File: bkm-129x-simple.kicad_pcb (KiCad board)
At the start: 2 copper layers, 105 x 160 mm, 55 parts, among them J1 YG_IN, J11 YG_OUT, J2 PBB_IN, J21 PBB_OUT, J3 PRR_IN, J31 PRR_OUT, J4 SYNC_IN, J41 SYNC_OUT, J5 Conn_02x32_Row_Letter_Last, Q1 DTC144EKA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

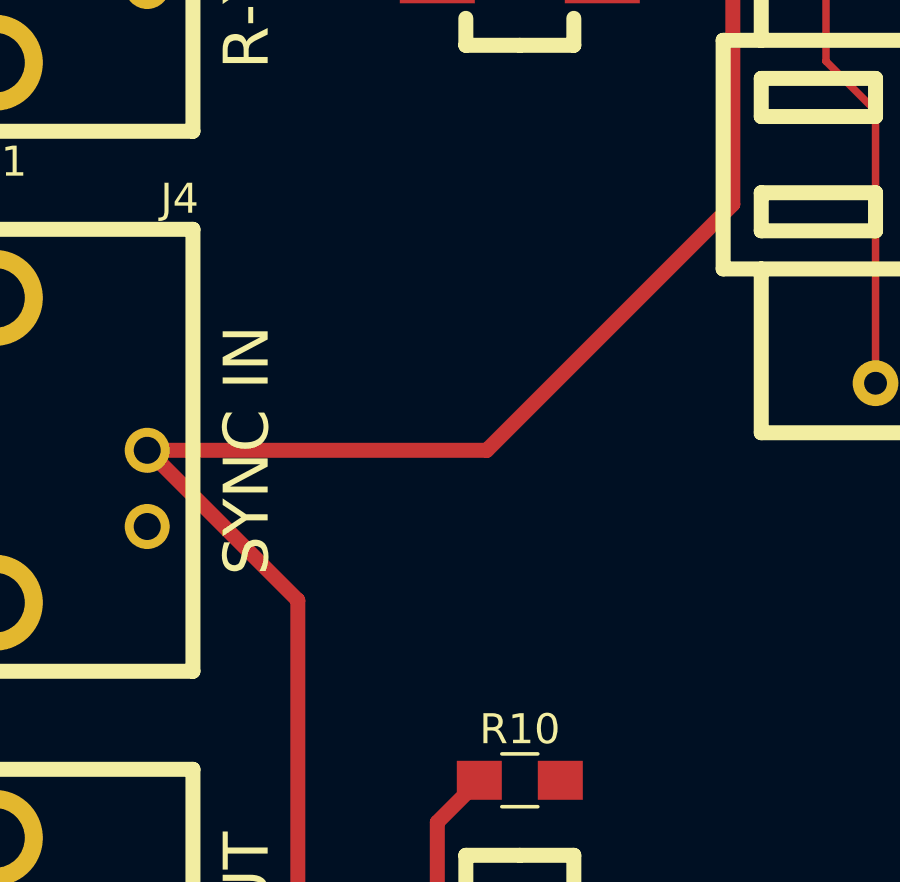
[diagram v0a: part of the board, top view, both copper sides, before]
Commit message: Add sync level info
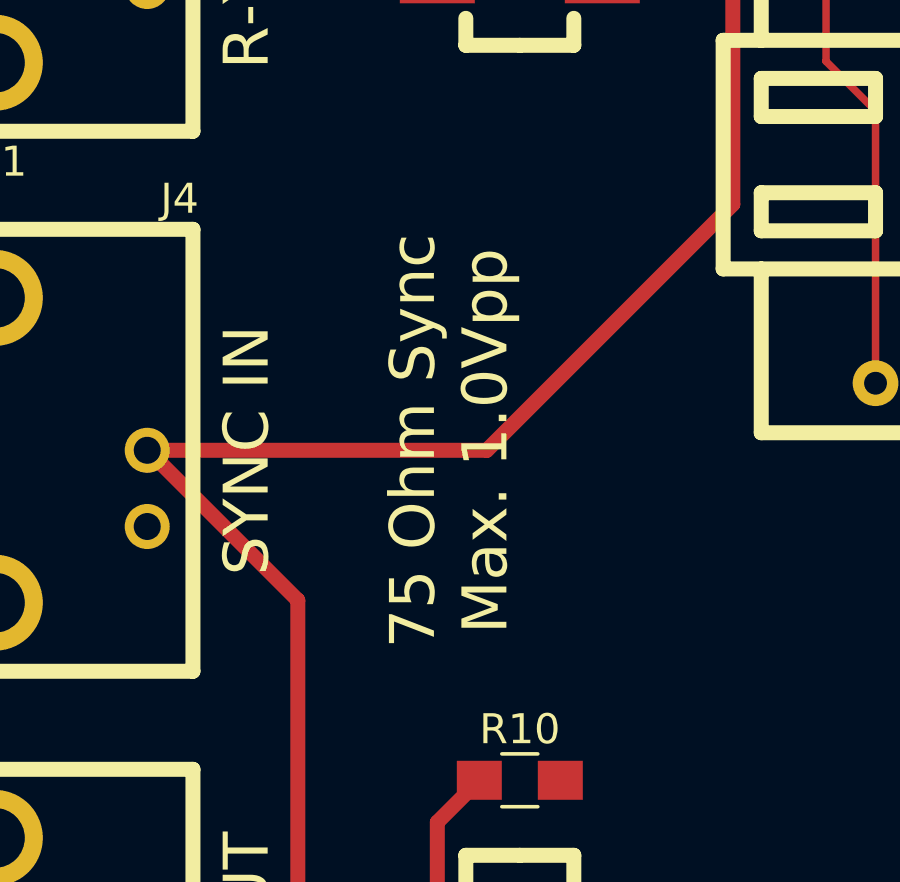
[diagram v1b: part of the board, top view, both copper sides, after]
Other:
- board text added: "75 Ohm Sync Max. 1.0Vpp"
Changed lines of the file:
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@@
     (area 73.555999 43.324999 201.918 203.475001)
     (thickness 1.6)
-    (drawings 25)
+    (drawings 26)
     (tracks 432)
     (zones 0)
@@
     (pad 4 smd rect (at -2.5 -2.75 270) (size 1.2 2.5) (layers F.Cu F.Paste F.Mask))
   )
+  (gr_text "75 Ohm Sync\nMax. 1.0Vpp" (at 117.35 168.09 90) (layer F.SilkS)
+    (effects (font (size 1.5 1.5) (thickness 0.3)))
+  )
   (gr_text "ON (75R TERM)\n\nOFF (PASSTHROUGH)" (at 126.2 78.4) (layer F.SilkS)

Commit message: Rev B: Added onboard MCU
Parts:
- added C15: 1uF, Capacitors_SMD:C_0805_HandSoldering, F.Cu at (140.8, 161.5)
- added C16: 4.7uF, Capacitors_SMD:C_0805_HandSoldering, F.Cu at (157.6, 155.4)
- added C17: 100nF, Capacitors_SMD:C_0805_HandSoldering, F.Cu at (142.0, 163.7)
- added J6: ICSP, Pin_Headers:Pin_Header_Straight_2x03_Pitch2.54mm, F.Cu at (168.9, 161.1)
- added U6: ATMEGA328PB-AU, Housings_QFP:TQFP-32_7x7mm_Pitch0.8mm, F.Cu at (149.3, 158.5)
- added Y1: CSTNE16M0VH3L000R0, muRata-CSTNEx:CSTNEx, F.Cu at (153.6, 153.2)
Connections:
- net /MCU_SCK renamed MCU_SCK
- net /MCU_SLOT_ID renamed MCU_SLOT_ID
- net /~MCU_RESET renamed ~MCU_RESET
- net Net-(R23-Pad1) renamed MCU_MISO
- net Net-(U3-Pad13) renamed ~MCU_SS
- net Net-(U3-Pad14) renamed MCU_MOSI
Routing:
- net MCU_SCK: track 42.1 -> 110.1 mm
- net MCU_MISO: track 30.6 -> 73.1 mm, vias 1 -> 2
- net MCU_MOSI: track 16.0 -> 53.3 mm, vias 0 -> 1
- net +5VD: track 102.4 -> 136.2 mm
- net ~MCU_RESET: track 17.8 -> 39.4 mm
- net ~MCU_SS: track 25.3 -> 36.5 mm
- net MCU_SLOT_ID: track 21.3 -> 31.0 mm, vias 1 -> 2
- net Net-(U6-Pad7): track 0.00 -> 5.31 mm
- net ~EXT_SYNC_OE: track 35.5 -> 40.4 mm
- net Net-(C17-Pad2): track 0.00 -> 4.14 mm
- net ~BX_OE: track 46.4 -> 49.9 mm
- net Net-(U6-Pad8): track 0.00 -> 3.21 mm
- net GND: track 10.6 -> 11.9 mm, vias 8 -> 9
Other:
- board text added: "ICSP"
- board text added: "Only mount inside this area, if NOT using a premade Arduino Nano board! U6 - ATMEGA328PB-AU Y1 - CSTNE16M0VH3L000R0 (16MHz resonator, GND in middle) C15 - 1 uF C16 - 4.7 uF C17 - 0.1 uF"
- board text added: "Rev. B"
- board text removed: "Rev. A"

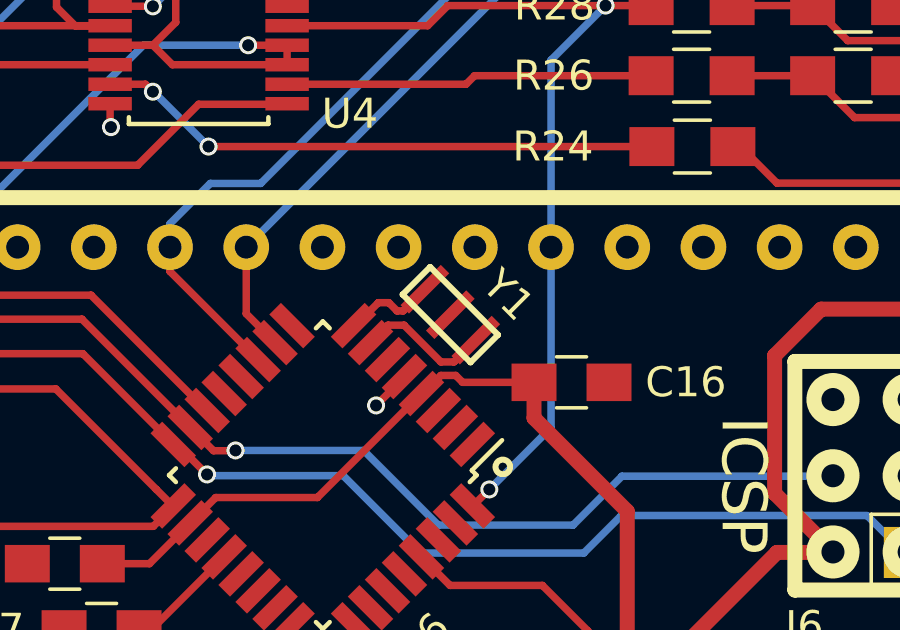
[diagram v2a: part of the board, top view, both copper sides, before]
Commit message: Add onboard ATMEGA328PB
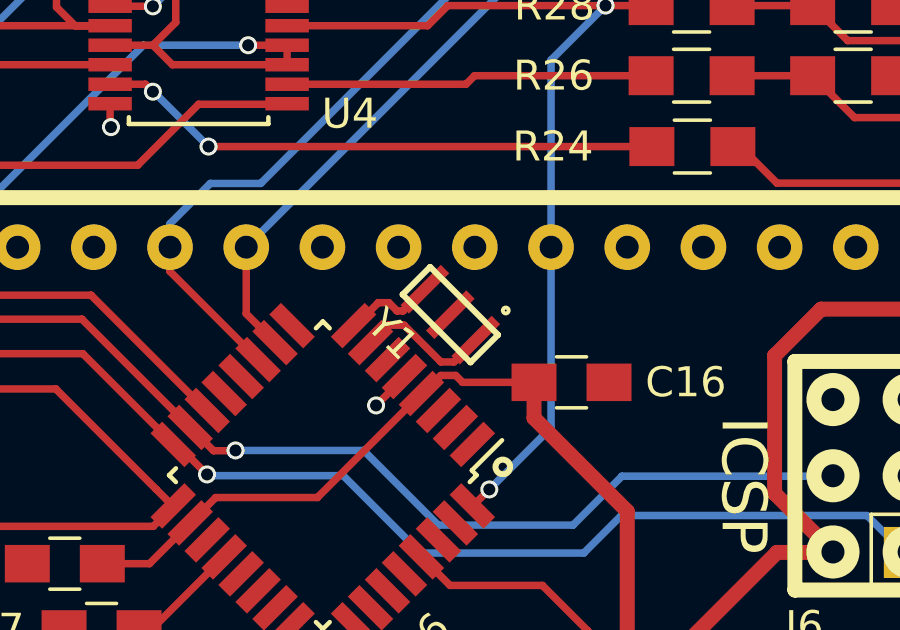
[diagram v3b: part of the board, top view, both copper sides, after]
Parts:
- turned Y1 to 135 degrees
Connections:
- Y1 pad 1: Net-(U6-Pad8) -> Net-(U6-Pad7)
- Y1 pad 3: Net-(U6-Pad7) -> Net-(U6-Pad8)
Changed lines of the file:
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@@
     (links 194)
     (no_connects 0)
-    (area 73.555999 43.324999 201.918 203.475001)
+    (area 94.124999 43.324999 199.275001 203.475001)
     (thickness 1.6)
-    (drawings 34)
+    (drawings 35)
     (tracks 543)
     (zones 0)
@@
   )
   (module muRata-CSTNEx:CSTNEx (layer F.Cu)
-    (at 153.6 153.175 315)
-    (fp_text reference Y1 (at 0.901561 -1.827871 315) (layer F.SilkS)
+    (at 153.6 153.175 135)
+    (fp_text reference Y1 (at 0.901561 -1.827871 135) (layer F.SilkS)
       (effects (font (size 1 1) (thickness 0.15)))
     )
-    (fp_text value CSTNE16M0VH3L000R0 (at 0 -1.6 315) (layer F.Fab)
+    (fp_text value CSTNE16M0VH3L000R0 (at 0 -1.6 135) (layer F.Fab)
       (effects (font (size 1 1) (thickness 0.15)))
     )
@@
     (fp_line (start -1.6 0.65) (end 1.6 0.65) (layer F.SilkS) (width 0.2))
     (fp_line (start 1.6 0.65) (end 1.6 -0.65) (layer F.SilkS) (width 0.2))
-    (pad 2 smd rect (at 0 0 315) (size 0.4 1.9) (layers F.Cu F.Paste F.Mask)
+    (pad 2 smd rect (at 0 0 135) (size 0.4 1.9) (layers F.Cu F.Paste F.Mask)
       (net 10 GND))
-    (pad 3 smd rect (at 1.2 0 315) (size 0.4 1.9) (layers F.Cu F.Paste F.Mask)
-      (net 52 "Net-(U6-Pad7)"))
-    (pad 1 smd rect (at -1.2 0 315) (size 0.4 1.9) (layers F.Cu F.Paste F.Mask)
+    (pad 3 smd rect (at 1.2 0 135) (size 0.4 1.9) (layers F.Cu F.Paste F.Mask)
       (net 53 "Net-(U6-Pad8)"))
+    (pad 1 smd rect (at -1.2 0 135) (size 0.4 1.9) (layers F.Cu F.Paste F.Mask)
+      (net 52 "Net-(U6-Pad7)"))
   )
   (module Pin_Headers:Pin_Header_Straight_2x03_Pitch2.54mm (layer F.Cu)
@@
     )
   )
+  (gr_circle (center 155.448 153.035) (end 155.5115 153.035) (layer F.SilkS) (width 0.2))
   (gr_text ICSP (at 163.37 158.86 270) (layer F.SilkS)
     (effects (font (size 1.5 1.5) (thickness 0.3)))
@@
   (segment (start 154.523528 153.948528) (end 154.47647 153.948528) (width 0.25) (layer F.Cu) (net 52))
   (segment (start 154.47647 153.948528) (end 153.974998 154.45) (width 0.25) (layer F.Cu) (net 52))
+  (segment (start 152.027944 153.05) (end 152.826472 152.251472) (width 0.25) (layer F.Cu) (net 53))
   (segment (start 150.375305 153.539897) (end 150.435103 153.539897) (width 0.25) (layer F.Cu) (net 53))
   (segment (start 150.435103 153.539897) (end 151.2 152.775) (width 0.25) (layer F.Cu) (net 53))
@@
   (segment (start 151.55 152.775) (end 151.825 153.05) (width 0.25) (layer F.Cu) (net 53))
   (segment (start 151.825 153.05) (end 152.027944 153.05) (width 0.25) (layer F.Cu) (net 53))
-  (segment (start 152.027944 153.05) (end 152.826472 152.251472) (width 0.25) (layer F.Cu) (net 53))
   (segment (start 143.225 163.65) (end 143.659314 163.65) (width 0.25) (layer F.Cu) (net 54))
   (segment (start 143.659314 163.65) (end 146.061953 161.247361) (width 0.25) (layer F.Cu) (net 54))

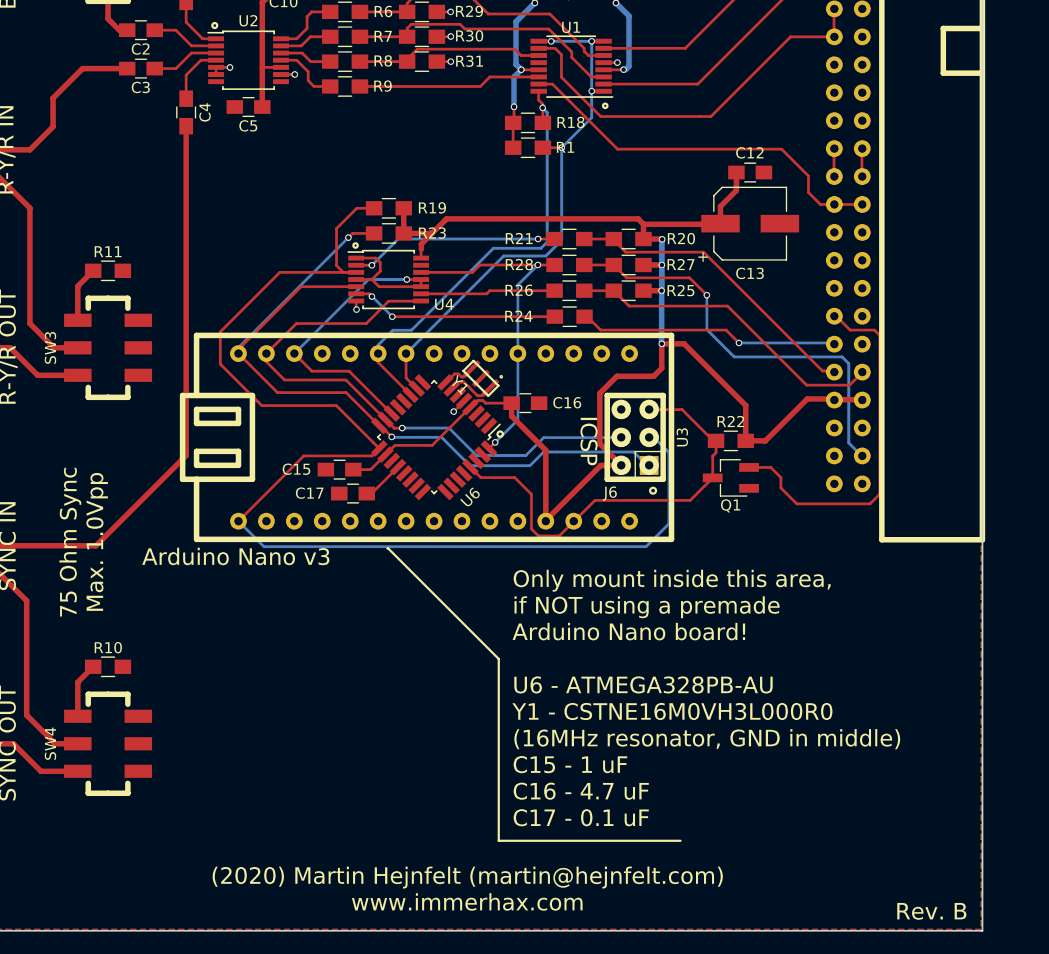
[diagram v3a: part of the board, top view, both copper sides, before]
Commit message: Fixed the THS7374 filter stuff, moved to Kicad 5
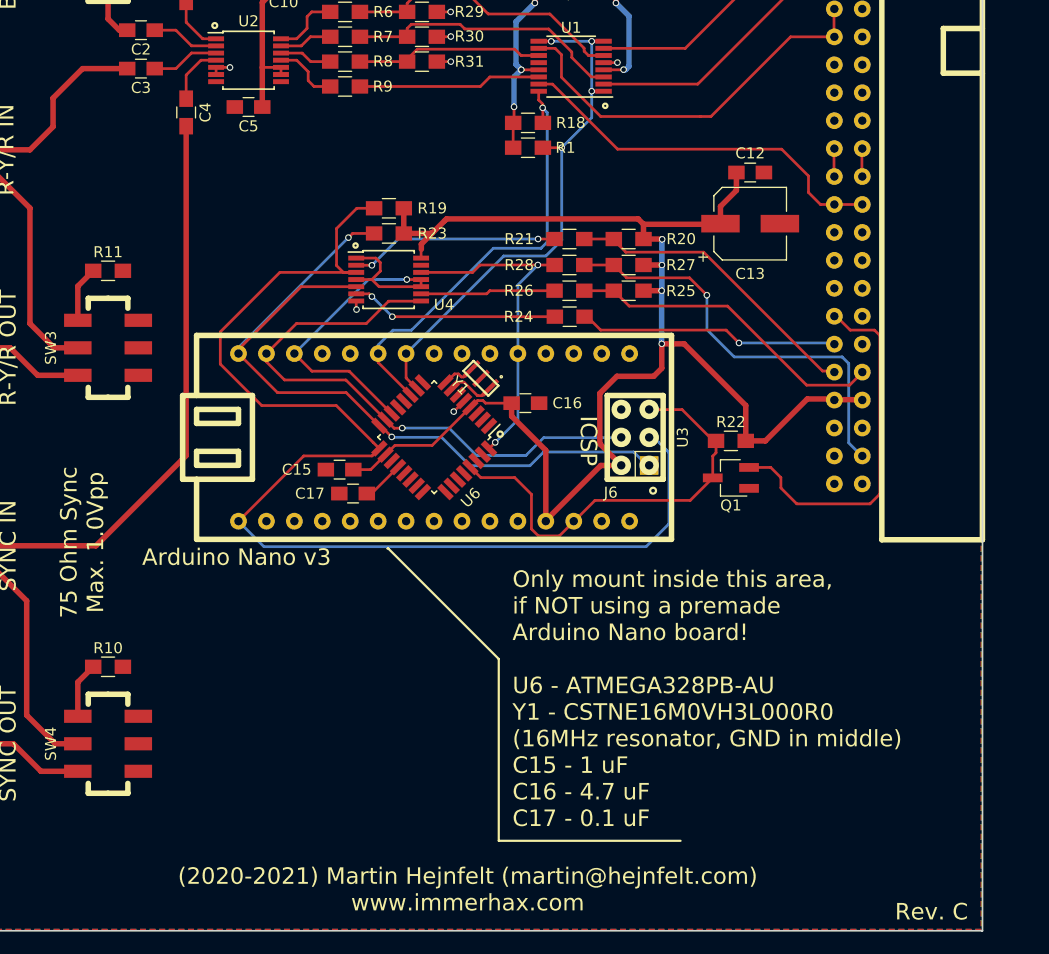
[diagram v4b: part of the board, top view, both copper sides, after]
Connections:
- U2 pad 9: GND -> +3V3
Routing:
- net GND: track 11.9 -> 10.7 mm, vias 9 -> 8
- net +3V3: track 16.0 -> 16.7 mm
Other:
- rule pad_to_mask_clearance: 0.2 -> 0
- board text added: "(2020-2021) Martin Hejnfelt (martin@hejnfelt.com) www.immerhax.com"
- board text added: "Rev. C"
- board text removed: "(2020) Martin Hejnfelt (martin@hejnfelt.com) www.immerhax.com"
- board text removed: "Rev. B"

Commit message: Revision D
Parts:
- added C101: 1uF, Capacitor_SMD:C_0805_2012Metric_Pad1.18x1.45mm_HandSolder, F.Cu at (140.5, 116.4)
- added C102: 4.7uF, Capacitor_SMD:C_0805_2012Metric_Pad1.18x1.45mm_HandSolder, F.Cu at (150.2, 110.8)
- added U101: LD1117S33TR_SOT223, Package_TO_SOT_SMD:SOT-223-3_TabPin2, F.Cu at (143.7, 110.8)
- C1, C10, C11, C12, C15, C16, C17, C2, C3, C4, C5, C6, C9: footprint Capacitors_SMD:C_0805_HandSoldering -> Capacitor_SMD:C_0805_2012Metric_Pad1.18x1.45mm_HandSolder
- C13, C7, C8: footprint Capacitors_SMD:CP_Elec_6.3x5.3 -> Capacitor_SMD:CP_Elec_6.3x5.3
- J5: footprint din-41612-64p-ra:DIN-41612-64P -> standard-pin-64p-ra:STANDARD-PIN-64P-RA
- Q1: footprint TO_SOT_Packages_SMD:SC-59_Handsoldering -> Package_TO_SOT_SMD:SC-59_Handsoldering
- R1, R10, R11, R12, R13, R18, R19, R20, R21, R22, R23, R24, R25, R26, R27, R28, R29, R30, R31, R6, R7, R8, R9: footprint Resistors_SMD:R_0805_HandSoldering -> Resistor_SMD:R_0805_2012Metric_Pad1.20x1.40mm_HandSolder
- U1: footprint Housings_SSOP:TSSOP-16_4.4x5mm_Pitch0.65mm -> Package_SO:TSSOP-16_4.4x5mm_P0.65mm
- U2, U4: footprint Housings_SSOP:TSSOP-14_4.4x5mm_Pitch0.65mm -> Package_SO:TSSOP-14_4.4x5mm_P0.65mm
- U5: footprint TO_SOT_Packages_SMD:SOT-23-5_HandSoldering -> Package_TO_SOT_SMD:SOT-23-5_HandSoldering
- U6: footprint Housings_QFP:TQFP-32_7x7mm_Pitch0.8mm -> Package_QFP:TQFP-32_7x7mm_P0.8mm
- moved C9 0.21 mm to (170.6, 114.3)
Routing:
- net +3V3: track 16.7 -> 41.7 mm
- net +5VD: track 136.2 -> 133.2 mm
- net VDD: track 85.1 -> 87.6 mm
- net GND: track 10.7 -> 9.33 mm, vias 8 -> 9
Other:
- board text added: "C7,8,13 - 100uF/16V 6,3x5,3 E-caps C10 - 2.2uF or C102 - 4.7uF C11 - 1.0uF or C101 - 1.0uF Rest - 0.1uF 0805 size"
- board text added: "ONLY MOUNT ONE OF THESE SECTIONS"
- board text added: "Rev. D"
- board text added: "U1 - ADG1611BRUZ or DG1411EEQ U2 - THS7374 U3 - Arduino Nano v3 U4 - 74VHC125 U5 - MIC3490-3.3 or U101 - LD1117S33TR Q1 - DTC144EKA U1/2/4: TSSOP14 SW1,2,3,4 - JS202011SCQN"
- board text removed: "C7,8,13 - 100uF/16V 6,3x5,3 E-caps C10 - 2.2uF C11 - 1.0uF Rest - 0.1uF 0805 size"
- board text removed: "Rev. C"
- board text removed: "U1 - ADG1611 U2 - THS7374 U3 - Arduino Nano v3 U4 - 74VHC125 U5 - MIC3490-3.3 Q1 - DTC144EKA U1/2/4: TSSOP14 SW1,2,3,4 - JS202011SCQN"
